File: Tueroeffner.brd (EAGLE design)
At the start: 54.6 x 22.9 mm, 34 parts, among them IC1 NCP1117ST33T3G, IC3 M25PE20, K1 EC2-12SNU, Q1 2N7002CK, Q3 2N7002CK

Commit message: New H-Bridge
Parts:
- removed D3, D4: PMBD914, semicon-smd-ipc:SOT23
- added Q2, Q4: 2N7002CK, SparkFun-DiscreteSemi:SOT23-3
- added R8, R9: 100, resistor:M2012
- R4, R5: value 47 -> 10K
- moved R1 26.5 mm to (45.4, 18.6), turned to 270 degrees
- moved SV3 26.0 mm to (17.6, 18.6), turned to 180 degrees
- moved U$1 18.5 mm to (39.2, 17.6), turned to 180 degrees
- moved LED4 16.7 mm to (22.7, 11.7), flipped to the top, turned to 90 degrees
- moved R32 12.7 mm to (22.7, 13.8), flipped to the top
- moved C5 9.94 mm to (33.0, 18.6), turned to 270 degrees
- moved D2 7.73 mm to (13.5, 1.11), turned to 90 degrees
- moved R6 3.76 mm to (39.4, 12.1)
- moved Q3 3.49 mm to (35.6, 12.1), turned to 90 degrees
- moved Q1 3.30 mm to (35.4, 1.27)
- moved JP2 3.02 mm to (0.48, 4.68)
- moved JP3 3.02 mm to (50.6, 4.68)
- moved R7 2.63 mm to (39.2, 1.27)
- moved R4 2.63 mm to (28.9, 11.7), turned to 270 degrees
- moved C3 2.51 mm to (12.5, 13.7), turned to 0 degrees
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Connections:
- new net N$4: R8.2, U$5.14
- new net N$5: R9.2, U$5.13
- net DC_5-12V: now also Q2.3, Q4.3; no longer D3.3, D4.3, R4.2, R5.2
- net GND: now also R4.1, R5.1
- net N$2: now also Q2.2; no longer D3.1, R4.1
- net N$3: now also Q4.2; no longer D4.1, R5.1
- net RELAY0: now also Q2.1, R4.2, R8.1; no longer U$5.14
- net RELAY1: now also Q4.1, R5.2, R9.1; no longer U$5.13
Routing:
- net VCC-3.3V: track 92.0 -> 0.00 mm, vias 3 -> 0
- net DC_5-12V: track 80.1 -> 0.00 mm
- net MOSI: track 56.8 -> 0.00 mm, vias 5 -> 0
- net MISO: track 50.4 -> 0.00 mm, vias 3 -> 0
- net RXD: track 50.3 -> 0.00 mm, vias 4 -> 0
- net SCK: track 49.9 -> 0.00 mm
- net INT1: track 37.5 -> 0.00 mm, vias 1 -> 0
- net RELAY0: track 30.7 -> 0.00 mm, vias 3 -> 0
- net RESET: track 30.3 -> 0.00 mm, vias 2 -> 0
- net TXD: track 26.8 -> 0.00 mm
- net CS: track 19.9 -> 0.00 mm
- net BUTTON: track 19.2 -> 0.00 mm, vias 1 -> 0
- net RELAY1: track 18.5 -> 0.00 mm, vias 1 -> 0
- net RELAY: track 13.2 -> 0.00 mm
- net AC_5-12V0: track 10.0 -> 0.00 mm, vias 1 -> 0
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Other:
- board text added: "Reroute Connectors 5.02"

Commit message: Basic Routing
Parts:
- removed R5, R7: 10K, resistor:M2012
- moved D2 36.5 mm to (45.4, 18.9), flipped to the top
- moved LED4 17.9 mm to (4.76, 11.7), flipped to the bottom, turned to 270 degrees
- moved R6 15.3 mm to (25.7, 5.24)
- moved R32 14.0 mm to (8.89, 11.7), flipped to the bottom
- moved Q4 11.6 mm to (30.0, 12.7)
- moved Q3 9.76 mm to (26.5, 8.41), turned to 0 degrees
- moved Q1 8.95 mm to (30.0, 8.41), turned to 0 degrees
- moved R4 6.60 mm to (30.0, 5.24), turned to 180 degrees
- moved Q2 5.91 mm to (26.5, 12.7)
- moved R8 5.54 mm to (30.0, 3.17)
- moved SV3 3.65 mm to (14.0, 18.6)
- moved R9 3.49 mm to (25.7, 3.17), turned to 0 degrees
- moved JP1 3.17 mm to (30.0, 19.2)
- moved K1 2.98 mm to (39.7, 9.37)
- moved JP3 2.12 mm to (51.0, 2.62)
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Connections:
- net GND: no longer R5.1, R7.1
- net RELAY0: no longer R7.2
- net RELAY1: no longer R5.2
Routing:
- net DC_5-12V: track 0.00 -> 68.1 mm
- net VCC-3.3V: track 0.00 -> 23.1 mm
- net RELAY1: track 0.00 -> 15.2 mm
- net BUTTON: track 0.00 -> 13.2 mm
- net RELAY0: track 0.00 -> 11.2 mm
- net N$2: track 0.00 -> 11.2 mm
- net N$33: track 0.00 -> 10.7 mm
- net N$3: track 0.00 -> 7.05 mm
- net RELAY: track 0.00 -> 5.08 mm
- net INT1: track 0.00 -> 4.67 mm
- net ANTENNA: track 0.00 -> 4.48 mm
- net N$1: track 0.00 -> 2.36 mm
- net RESET: track 0.00 -> 2.21 mm
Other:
- board text removed: "Reroute Connectors 5.02"

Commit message: RC 2.0
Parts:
- moved C5 14.4 mm to (48.3, 17.0)
- moved D2 12.3 mm to (33.2, 17.6), flipped to the bottom, turned to 180 degrees
- moved C6 10.0 mm to (5.08, 12.7), turned to 270 degrees
- moved LED4 4.48 mm to (8.89, 13.5)
- moved JP1 3.02 mm to (30.0, 16.2)
- moved L2 2.54 mm to (26.4, 16.4)
- moved R2 0.97 mm to (8.32, 0.56)
- moved C7 0.50 mm to (14.7, 4.21)
- turned R3 to 0 degrees
- turned R32 to 180 degrees
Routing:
- net VCC-3.3V: track 23.1 -> 141.1 mm, vias 0 -> 4
- net INT1: track 4.67 -> 46.3 mm
- net MISO: track 0.00 -> 38.9 mm, vias 0 -> 2
- net BUTTON: track 13.2 -> 48.3 mm
- net N$4: track 0.00 -> 30.3 mm, vias 0 -> 1
- net SCK: track 0.00 -> 22.3 mm
- net RESET: track 2.21 -> 22.9 mm, vias 0 -> 2
- net N$5: track 0.00 -> 19.0 mm, vias 0 -> 1
- net CS: track 0.00 -> 17.9 mm
- net MOSI: track 0.00 -> 15.9 mm
- net RXD: track 0.00 -> 14.8 mm
- net AC_5-12V0: track 0.00 -> 12.4 mm
- net TXD: track 0.00 -> 12.4 mm
- net DC_5-12V: track 68.1 -> 80.1 mm
- net RELAY: track 5.08 -> 12.9 mm
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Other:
- board text added: "Zwave-Europe (GER) 2016 S.Schreiter DoorOpener"
- board text removed: "Zwave-Europe (GER) 2015 S.Schreiter DoorOpener"

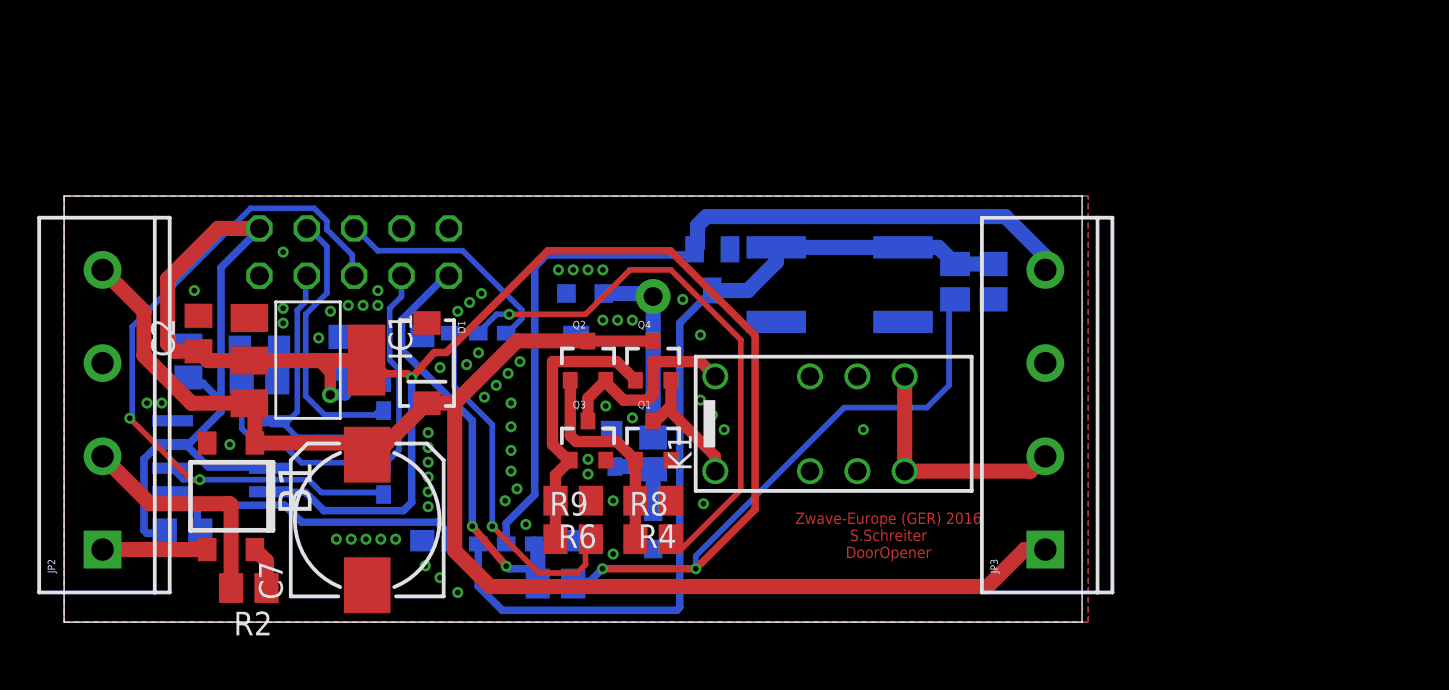
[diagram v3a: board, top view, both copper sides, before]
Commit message: New Relais designe
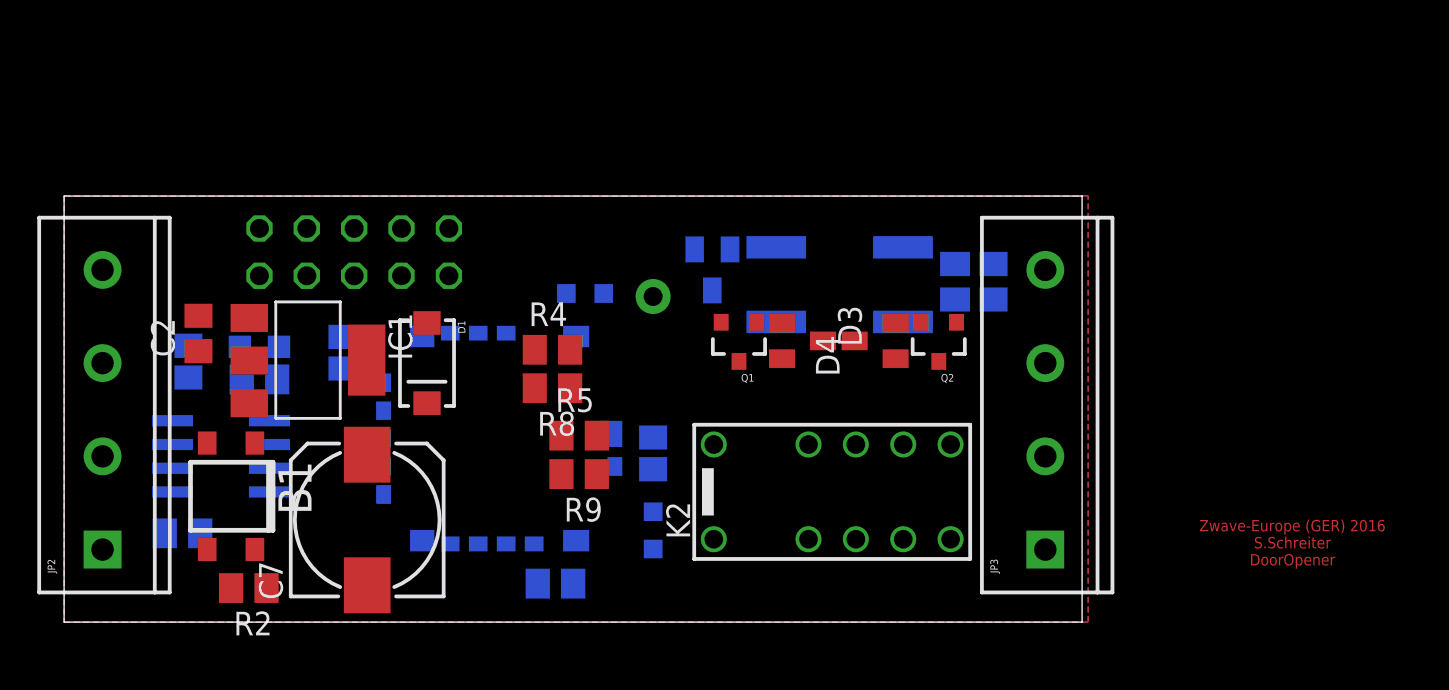
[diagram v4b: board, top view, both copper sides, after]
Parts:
- removed K1: EC2-12SNU, relay:TXD2
- removed Q3, Q4: 2N7002CK, SparkFun-DiscreteSemi:SOT23-3
- removed R6: 10K, resistor:M2012
- added D3, D4: PMBD914, semicon-smd-ipc:SOT23
- added K2: EC2-12TNU, relay:TX2-L2
- added R5: 10K, resistor:M2012
- moved Q2 18.8 mm to (45.3, 13.8), turned to 180 degrees
- moved R4 9.73 mm to (24.6, 13.3), turned to 0 degrees
- moved R8 9.73 mm to (24.6, 11.3), turned to 180 degrees
- moved Q1 7.09 mm to (34.6, 13.8), turned to 180 degrees
- moved R9 3.51 mm to (26.0, 6.67), turned to 180 degrees
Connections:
- removed net N$2: K1.12, Q2.2, Q3.3
- removed net N$3: K1.1, Q1.3, Q4.2
- new net N$6: D3.1, K2.12, Q1.3
- new net N$7: D4.1, K2.7, Q2.3
- net DC_5-12V: now also D3.3, D4.3, K2.1, K2.5, K2.6, K2.8; no longer Q2.3, Q4.3
- net GND: now also K2.10, K2.3, Q2.2, R5.1; no longer K1.4, K1.9, Q3.2, R6.1
- net RELAY: now also K2.4, K2.9; no longer K1.5, K1.8
- net RELAY0: no longer Q2.1
- net RELAY1: now also Q2.1, R5.2; no longer Q3.1, Q4.1, R6.2
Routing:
- net VCC-3.3V: track 141.1 -> 0.00 mm, vias 4 -> 0
- net DC_5-12V: track 80.1 -> 0.00 mm
- net BUTTON: track 48.3 -> 0.00 mm
- net INT1: track 46.3 -> 0.00 mm
- net MISO: track 38.9 -> 0.00 mm, vias 2 -> 0
- net N$4: track 30.3 -> 0.00 mm, vias 1 -> 0
- net RESET: track 22.9 -> 0.00 mm, vias 2 -> 0
- net SCK: track 22.3 -> 0.00 mm
- net N$5: track 19.0 -> 0.00 mm, vias 1 -> 0
- net CS: track 17.9 -> 0.00 mm
- net MOSI: track 15.9 -> 0.00 mm
- net RELAY1: track 15.2 -> 0.00 mm
- net RXD: track 14.8 -> 0.00 mm
- net RELAY: track 12.9 -> 0.00 mm
- net AC_5-12V0: track 12.4 -> 0.00 mm
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
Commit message: Semi Routed
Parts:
- C7: value 470µF 16V -> 470µF 25V
- moved C5 40.6 mm to (7.70, 17.9), turned to 90 degrees
- moved R1 36.4 mm to (9.76, 17.9), turned to 90 degrees
- moved U$1 24.1 mm to (16.0, 18.0), turned to 0 degrees
- moved Q2 19.5 mm to (25.8, 14.5), turned to 270 degrees
- moved SV3 19.2 mm to (33.2, 18.2), turned to 0 degrees
- moved D4 16.3 mm to (25.8, 11.1), turned to 180 degrees
- moved D3 13.9 mm to (25.8, 7.22), turned to 0 degrees
- moved R9 13.6 mm to (19.3, 18.5)
- moved Q1 13.3 mm to (25.8, 3.81), turned to 270 degrees
- moved D2 10.4 mm to (22.8, 17.2), turned to 0 degrees
- moved D1 10.4 mm to (13.0, 3.41)
- moved R5 10.2 mm to (19.3, 16.4)
- moved C2 7.61 mm to (7.48, 6.83), turned to 270 degrees
- moved R2 7.00 mm to (5.24, 6.84), turned to 90 degrees
- moved JP3 6.98 mm to (44.1, 2.62)
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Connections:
- net AC_5-12V1: now also B1.AC1; no longer B1.AC2
- net N$1: now also B1.AC2; no longer B1.AC1
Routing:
- net DC_5-12V: track 0.00 -> 91.5 mm, vias 0 -> 1
- net VCC-3.3V: track 0.00 -> 42.6 mm
- net BUTTON: track 0.00 -> 35.0 mm
- net INT1: track 0.00 -> 14.4 mm
- net RELAY0: track 0.00 -> 13.6 mm
- net N$6: track 0.00 -> 11.2 mm
- net SCK: track 0.00 -> 10.9 mm
- net RELAY: track 0.00 -> 10.6 mm
- net N$7: track 0.00 -> 9.04 mm
- net RELAY1: track 0.00 -> 7.02 mm
- net MOSI: track 0.00 -> 5.97 mm
- net AC_5-12V1: track 0.00 -> 5.00 mm
- net AC_5-12V0: track 0.00 -> 4.83 mm
- net ANTENNA: track 0.00 -> 4.39 mm
- net N$33: track 0.00 -> 4.02 mm
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- added copper zone on layer 1, net VCC-3.3V

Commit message: Auto Router
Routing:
- net VCC-3.3V: track 42.6 -> 134.6 mm, vias 0 -> 1
- net MISO: track 0.00 -> 87.7 mm, vias 0 -> 2
- net RXD: track 0.00 -> 41.9 mm, vias 0 -> 1
- net SCK: track 10.9 -> 46.4 mm
- net MOSI: track 5.97 -> 37.9 mm, vias 0 -> 1
- net DC_5-12V: track 91.5 -> 113.3 mm
- net INT1: track 14.4 -> 35.7 mm
- net RESET: track 2.21 -> 21.1 mm, vias 0 -> 1
- net CS: track 0.00 -> 17.2 mm, vias 0 -> 2
- net TXD: track 0.00 -> 14.8 mm
- net N$5: track 0.00 -> 7.34 mm, vias 0 -> 1
- net N$4: track 0.00 -> 5.90 mm, vias 0 -> 1

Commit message: RC candidate
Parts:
- removed SV3: (no value), con-lstb:MA05-2
- added TP1, TP2, TP3, TP4, TP5, TP6, TP7, TP8: TPB1,27, testpad:B1,27
- moved JP1 7.94 mm to (30.3, 18.0)
- moved R4 6.58 mm to (25.8, 13.4)
- moved R5 6.58 mm to (25.8, 15.5)
- moved R8 6.58 mm to (25.8, 11.4)
- moved R9 6.58 mm to (25.8, 17.5)
- moved C7 5.18 mm to (24.0, 5.08)
- moved D3 5.00 mm to (30.8, 7.22)
- moved D4 4.05 mm to (29.8, 11.1)
- moved Q1 4.05 mm to (29.8, 3.81)
- moved Q2 4.05 mm to (29.8, 14.5)
- moved L2 3.99 mm to (27.3, 15.6), turned to 0 degrees
- moved C2 2.94 mm to (10.4, 6.75)
- moved R11 2.20 mm to (22.9, 0.64), turned to 0 degrees
- moved R3 2.01 mm to (9.84, 3.33)
- moved IC3 1.75 mm to (9.60, 7.38)
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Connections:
- net GND: now also TP4.TP; no longer SV3.7, SV3.9
- net MISO: now also TP6.TP; no longer SV3.6
- net MOSI: now also TP5.TP; no longer SV3.4
- net RESET: now also TP7.TP; no longer SV3.10
- net RXD: now also TP2.TP; no longer SV3.3
- net SCK: now also TP8.TP; no longer SV3.8
- net TXD: now also TP3.TP; no longer SV3.5
- net VCC-3.3V: now also TP1.TP; no longer SV3.1
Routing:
- net VCC-3.3V: track 134.6 -> 64.5 mm, vias 1 -> 5
- net MISO: track 87.7 -> 20.8 mm, vias 2 -> 3
- net RXD: track 41.9 -> 3.16 mm
- net SCK: track 46.4 -> 14.2 mm, vias 0 -> 1
- net MOSI: track 37.9 -> 7.34 mm
- net N$33: track 4.02 -> 12.0 mm
- net TXD: track 14.8 -> 8.65 mm, vias 0 -> 1
- net CS: track 17.2 -> 23.1 mm
- net N$6: track 11.2 -> 6.78 mm
- net INT1: track 35.7 -> 40.2 mm
- net RELAY0: track 13.6 -> 9.52 mm
- net N$7: track 9.04 -> 5.43 mm
- net RESET: track 21.1 -> 17.8 mm
- net RELAY1: track 7.02 -> 4.16 mm
- net DC_5-12V: track 113.3 -> 111.0 mm
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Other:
- board size 54.6 x 22.9 mm -> 48.2 x 22.9 mm

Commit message: Clean Up
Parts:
- moved D1 0.08 mm to (13.0, 3.33)
- renumbered TP1 to VC, TP2 to RX, TP3 to TX, TP4 to GN, TP5 to MO, TP6 to MI, TP7 to RS, TP8 to SK
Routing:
- net MISO: track 20.8 -> 20.3 mm
